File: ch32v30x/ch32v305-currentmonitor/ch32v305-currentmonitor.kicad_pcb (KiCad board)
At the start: 2 copper layers, 89 parts, among them J1 PGM, J2 USB_C_Receptacle_USB2.0, J3 PGM, Q1 AO3401A-P, Q10 2N7002, Q11 2N7002, Q12 2N7002, Q13 2N7002, Q2 AO3401A-P, Q3 AO3401A-P, Q4 AO3401A-P, Q5 AO3401A-P, Q6 AO3401A-P, Q7 AO3401A-P, Q8 2N7002, Q9 2N7002, U2 OPA567, U3 CH32V305GBU6, U4 TLV9001IDCK, U5 XC6206P332MR, U6 XC6206P332MR, Y1 8MHz

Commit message: Update all parts from tonight
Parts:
- added C24: 10p, Capacitor_SMD:C_0402_1005Metric, F.Cu at (163.5, 69.1)
- added C25: 10p, Capacitor_SMD:C_0402_1005Metric, F.Cu at (153.2, 71.5)
- added C26: 10p, Capacitor_SMD:C_0402_1005Metric, F.Cu at (161.6, 66.7)
- added C27: 10p, Capacitor_SMD:C_0402_1005Metric, F.Cu at (163.9, 72.0)
- added C28: 10p, Capacitor_SMD:C_0402_1005Metric, F.Cu at (141.4, 72.5)
- added C29: 10p, Capacitor_SMD:C_0402_1005Metric, F.Cu at (148.3, 79.8)
- added C30: 10p, Capacitor_SMD:C_0402_1005Metric, F.Cu at (150.4, 82.8)
- added C31: 100n, Capacitor_SMD:C_0402_1005Metric, F.Cu at (146.5, 78.4)
- added C32: 10p, Capacitor_SMD:C_0402_1005Metric, F.Cu at (152.1, 86.2)
- added C33: 10p, Capacitor_SMD:C_0402_1005Metric, F.Cu at (148.0, 89.4)
- added C34: 10p, Capacitor_SMD:C_0402_1005Metric, F.Cu at (120.2, 75.8)
- added C35: 10p, Capacitor_SMD:C_0402_1005Metric, F.Cu at (121.1, 77.9)
- added TP6: HOLE, MountingHole:MountingHole_3.2mm_M3_Pad_Via, F.Cu at (161.9, 85.3)
- added TP7: HOLE, MountingHole:MountingHole_3.2mm_M3_Pad_Via, F.Cu at (117.0, 70.4)
- added U7: USBLC6-2P6, Package_TO_SOT_SMD:SOT-666, F.Cu at (125.4, 69.9)
- J3: value PGM -> PWR
- moved Q7 109.0 mm to (175.0, 86.7), turned to 180 degrees
- moved Q6 108.7 mm to (175.0, 81.6), turned to 180 degrees
- moved Q13 107.9 mm to (180.9, 86.6), turned to 180 degrees
- moved Q12 107.8 mm to (181.0, 81.8), turned to 180 degrees
- moved Q11 107.7 mm to (181.1, 76.8), turned to 180 degrees
- moved Q5 105.2 mm to (175.0, 76.7), turned to 180 degrees
- moved Q10 105.1 mm to (180.9, 71.5), turned to 180 degrees
- moved Q4 105.0 mm to (174.9, 71.6), turned to 180 degrees
- moved Q9 105.0 mm to (180.8, 66.7), turned to 180 degrees
- moved Q3 104.8 mm to (174.8, 66.7), turned to 180 degrees
- moved Q8 104.7 mm to (180.6, 61.8), turned to 180 degrees
- moved Q2 104.7 mm to (174.7, 61.8), turned to 180 degrees
- moved R15 97.3 mm to (178.0, 87.7), turned to 180 degrees
- moved R23 96.3 mm to (183.5, 81.8), turned to 90 degrees
- moved R22 94.5 mm to (183.5, 86.5), turned to 90 degrees
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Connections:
- C3 pad 1: Net-(U1-VREFL2) -> GND
- C4 pad 2: Net-(U1-VREFL1) -> GND
- C5 pad 1: Net-(U1-VREFL2) -> GND
- C6 pad 2: Net-(U1-VREFL1) -> GND
- J3 pad 1: unconnected-(J3-Pin_1-Pad1) -> PARAIL
- J3 pad 2: GND -> PVA
- J3 pad 3: PVA -> GND
- Q10 pad 3: unconnected-(Q10-D-Pad3) -> Net-(Q10-D)
- R18 pad 2: unconnected-(R18-Pad2) -> Net-(Q10-D)
- U1 pad 11: Net-(U1-VREFL2) -> GND
- U1 pad 2: Net-(U1-VREFL1) -> GND
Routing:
- net GND: track 0.00 -> 288.8 mm, vias 0 -> 195
- net VNR: track 0.00 -> 108.6 mm, vias 0 -> 7
- net O0: track 0.00 -> 94.0 mm
- net O1: track 0.00 -> 87.4 mm
- net O2: track 0.00 -> 81.0 mm
- net PVA: track 0.00 -> 80.8 mm, vias 0 -> 9
- net PARAIL: track 0.00 -> 78.6 mm, vias 0 -> 8
- net O3: track 0.00 -> 74.4 mm
- net +5V: track 0.00 -> 73.9 mm, vias 0 -> 2
- net +3.3V: track 0.00 -> 72.8 mm, vias 0 -> 8
- net O4: track 0.00 -> 67.8 mm
- net O5: track 0.00 -> 60.2 mm
- net VOT: track 0.00 -> 48.4 mm, vias 0 -> 1
- net PD2AO: track 0.00 -> 29.2 mm, vias 0 -> 2
- net VSET: track 0.00 -> 28.8 mm, vias 0 -> 2
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- added copper zone on B.Cu, net GND
- added copper zone on F.Cu, net GND
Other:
- board outline added: 74 x 36 mm
- board text added: "RST SWC SWD GND 3V3"
- board text added: "ch32v305-currentmonitor cnhardware, rev -"

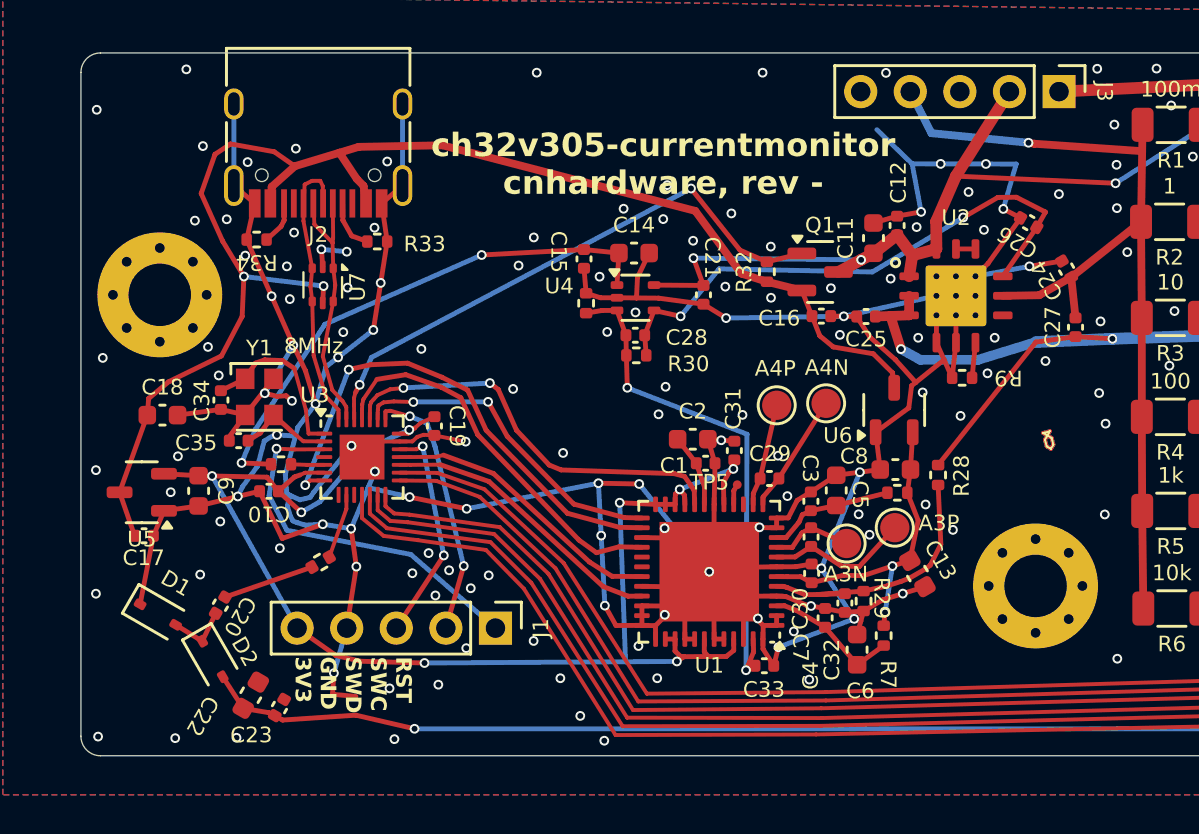
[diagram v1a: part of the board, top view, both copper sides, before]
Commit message: Bump to what was actually ordered
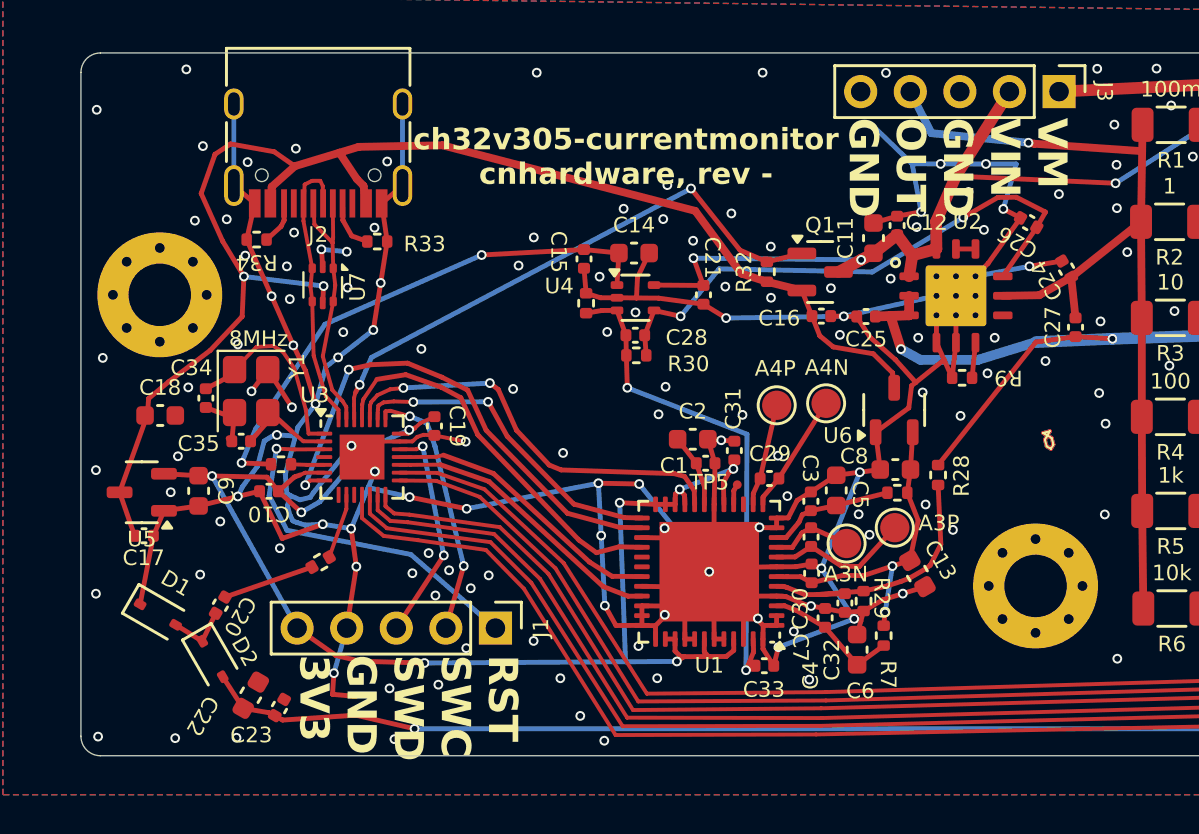
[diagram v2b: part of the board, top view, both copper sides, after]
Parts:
- Y1: footprint Oscillator:Oscillator_SMD_Kyocera_KC2520Z-4Pin_2.5x2.0mm -> Crystal:Crystal_SMD_3225-4Pin_3.2x2.5mm
- moved C34 0.78 mm to (119.4, 75.7)
- moved Y1 0.51 mm to (121.7, 75.3), turned to -90 degrees
- moved C35 0.13 mm to (121.2, 77.9)
- moved C18 0.12 mm to (117.1, 76.6)
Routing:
- net GND: track 288.8 -> 283.7 mm
- net Net-(U3-OSC_IN/PD0): track 8.72 -> 9.87 mm
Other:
- board text added: "VM VIN GND OUT GND"
